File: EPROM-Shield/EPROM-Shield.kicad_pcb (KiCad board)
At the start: 2 copper layers, 63.5 x 54.6 mm, 21 parts, among them J1 Conn_01x07, J2 Conn_01x06, J3 Conn_01x08, J4 Conn_01x06, U1 74LS595, U2 74LS595, U3 28C256

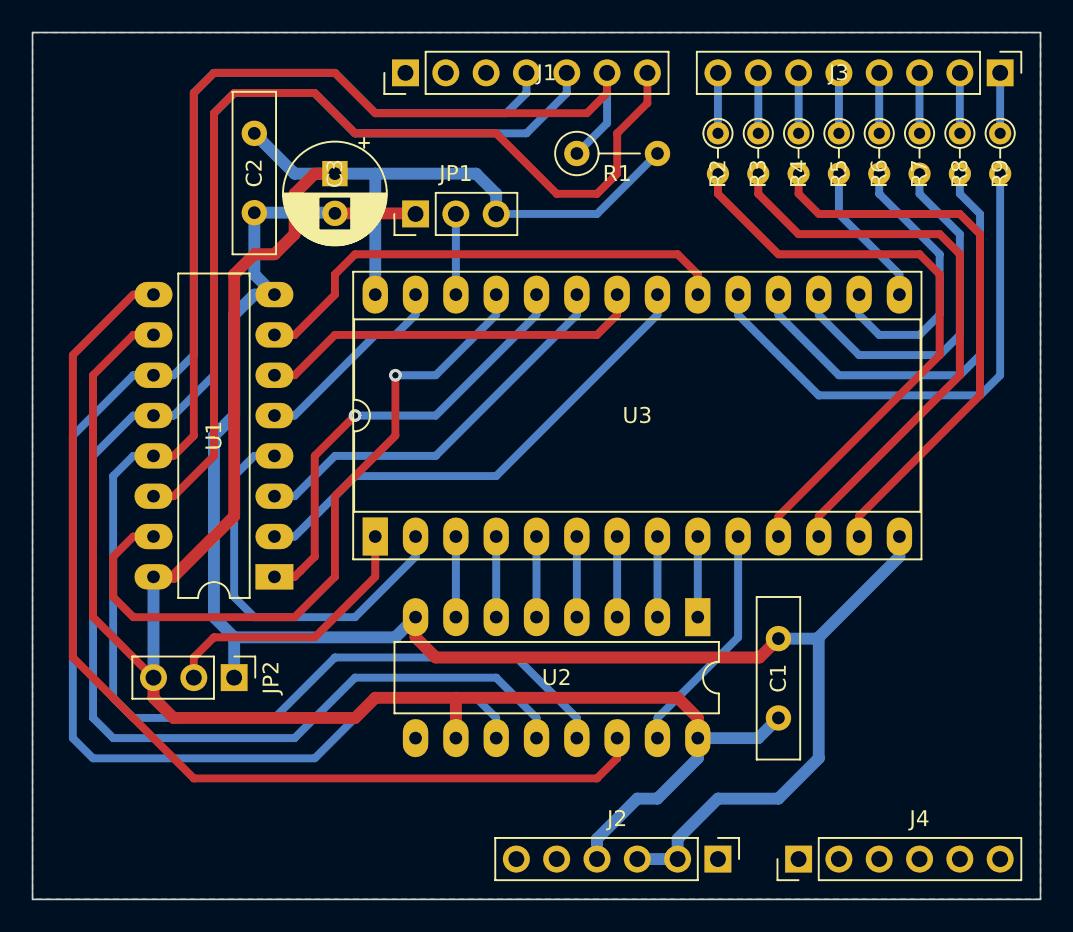
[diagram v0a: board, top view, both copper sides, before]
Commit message: EPROM-Shield: several fixes - more clear schematic with regards to the shift register control pins - fix the D0-D7 connections, resulting in smaller board - fix R values and positions
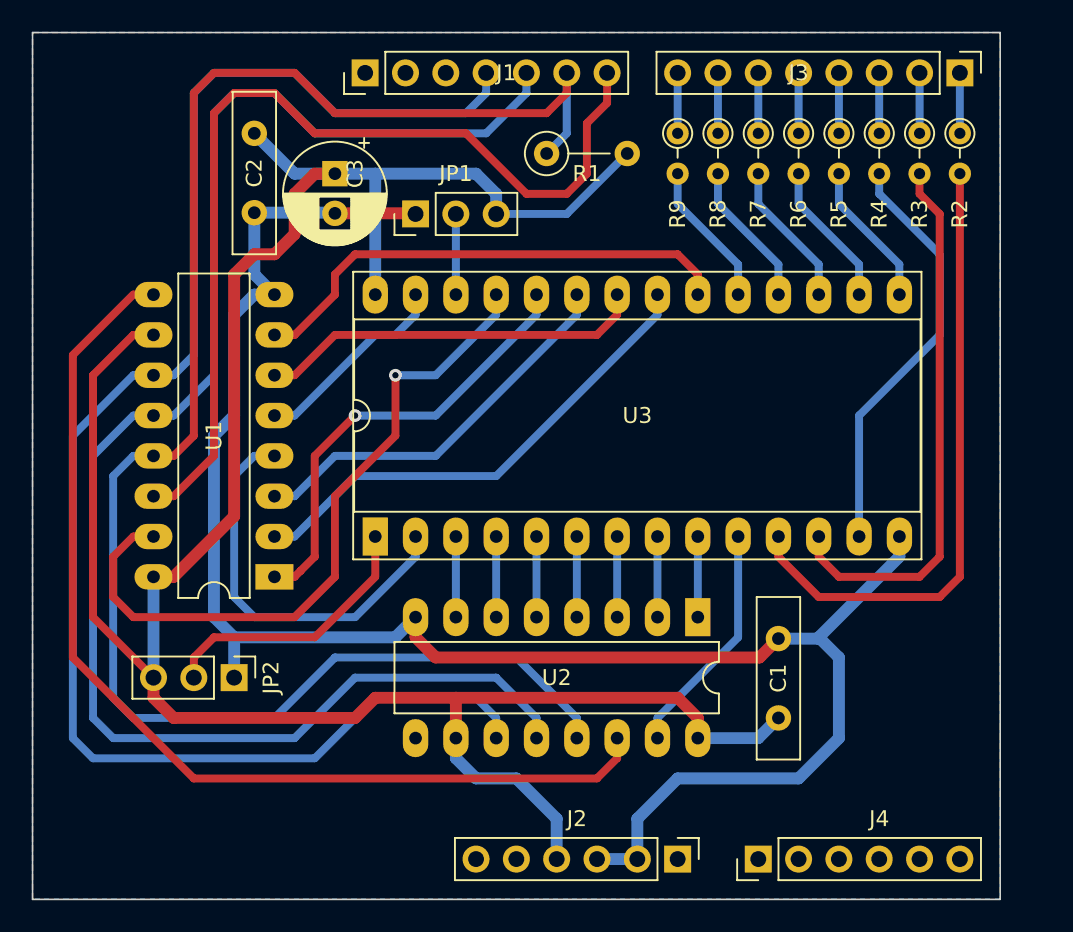
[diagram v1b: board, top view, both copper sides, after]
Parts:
- moved R9 20.3 mm to (127.0, 74.9)
- moved R2 15.2 mm to (144.8, 74.9)
- moved R8 15.2 mm to (129.5, 74.9)
- moved R3 10.2 mm to (142.2, 74.9)
- moved R7 10.2 mm to (132.1, 74.9)
- moved R4 5.08 mm to (139.7, 74.9)
- moved R6 5.08 mm to (134.6, 74.9)
- moved J1 2.54 mm to (107.3, 71.1)
- moved J2 2.54 mm to (127.0, 120.7)
- moved J3 2.54 mm to (144.8, 71.1)
- moved J4 2.54 mm to (132.1, 120.7)
- moved R1 1.91 mm to (118.7, 76.2)
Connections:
- net Net-(J1-Pad4) renamed /SERCLK
- net Net-(J1-Pad5) renamed /RCLK
- net Net-(J1-Pad6) renamed /_OE
- net Net-(J1-Pad7) renamed /SER
- J3 pad 1: /D7 -> /D0
- J3 pad 2: /D6 -> /D1
- J3 pad 3: /D5 -> /D2
- J3 pad 4: /D4 -> /D3
- J3 pad 5: /D3 -> /D4
- J3 pad 6: /D2 -> /D5
- J3 pad 7: /D1 -> /D6
- J3 pad 8: /D0 -> /D7
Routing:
- net Net-(R9-Pad2): track 33.1 -> 9.20 mm
- net Net-(R8-Pad2): track 28.0 -> 9.20 mm
- net Net-(R7-Pad2): track 23.0 -> 9.20 mm
- net Net-(R4-Pad2): track 36.0 -> 26.5 mm
- net Net-(R6-Pad2): track 17.9 -> 9.20 mm
- net GND: track 113.4 -> 117.7 mm
- net /_OE: track 111.1 -> 108.3 mm
- net /RCLK: track 101.2 -> 98.7 mm
- net /SERCLK: track 100.2 -> 97.6 mm
- net Net-(R3-Pad2): track 37.0 -> 34.6 mm
- net /SER: track 62.7 -> 60.5 mm
- net Net-(R2-Pad2): track 38.1 -> 39.7 mm
- net VCC: track 159.2 -> 158.0 mm
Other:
- board size 63.5 x 54.6 mm -> 61 x 54.6 mm
